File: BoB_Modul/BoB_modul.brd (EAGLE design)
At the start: 27.9 x 40.6 mm, 12 parts

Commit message: make metric and nice, not yet finnished, work in progress
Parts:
- moved C3 0.79 mm to (22.5, 17.5)
- moved X1 0.54 mm to (14.0, 40.1)
- moved R2 0.28 mm to (22.0, 10.0)
- moved C1 0.24 mm to (6.50, 4.00)
- moved R1 0.23 mm to (18.5, 5.50)
- moved C4 0.23 mm to (22.0, 7.00)
- moved LDO1 0.20 mm to (12.5, 7.00)
- moved SV2 0.16 mm to (25.5, 16.0)
- moved SV1 0.13 mm to (2.50, 16.0)
- moved LED1 0.09 mm to (18.5, 2.50)
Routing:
- net DBG_DATA_RX_LED: track 14.8 -> 0.00 mm, vias 1 -> 0
- net DBG_CLK_TX_LED: track 13.8 -> 0.00 mm, vias 1 -> 0
- net DBG_EN_NC: track 12.8 -> 0.00 mm, vias 1 -> 0
- net /RST: track 16.4 -> 15.3 mm
- net GND: track 45.9 -> 45.1 mm
- net GPIO2: track 8.24 -> 8.81 mm
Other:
- board size 27.9 x 40.6 mm -> 28 x 40 mm

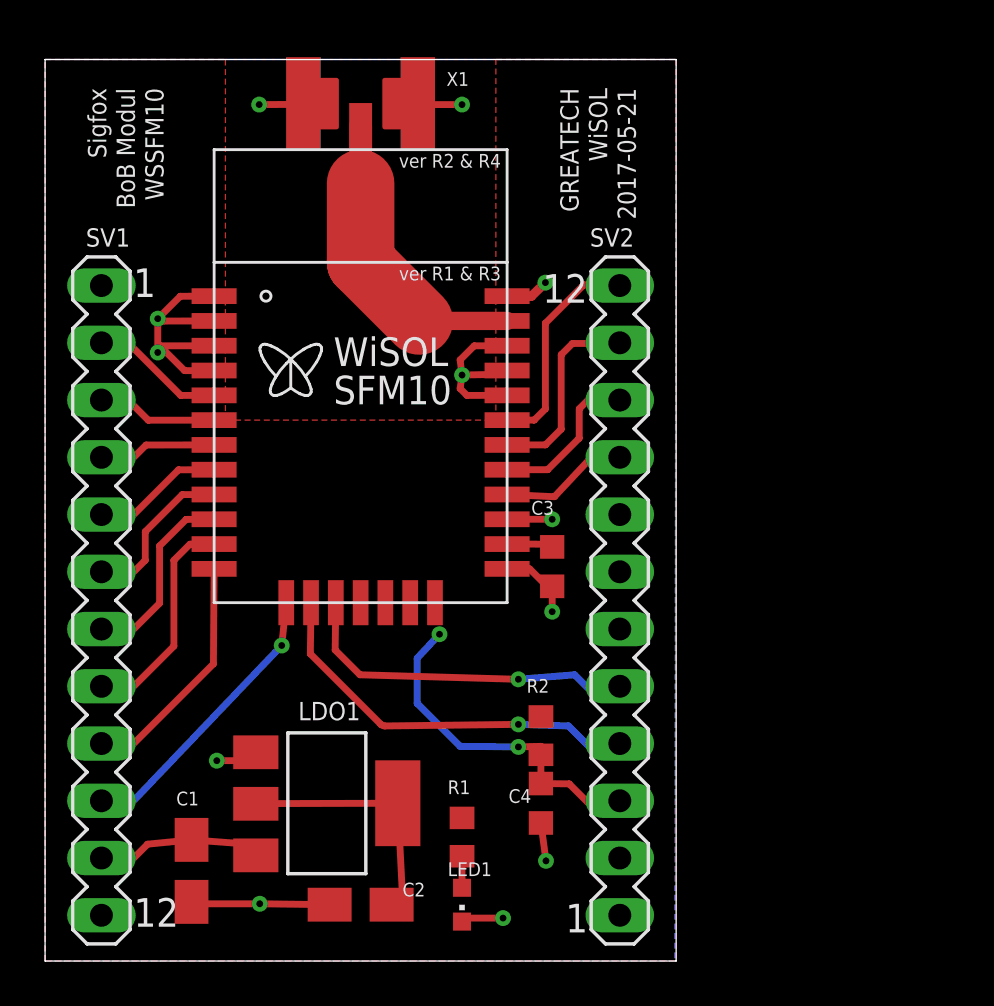
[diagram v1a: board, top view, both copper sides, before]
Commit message: make metric, moved vias out of WiSOL module, ready fro production
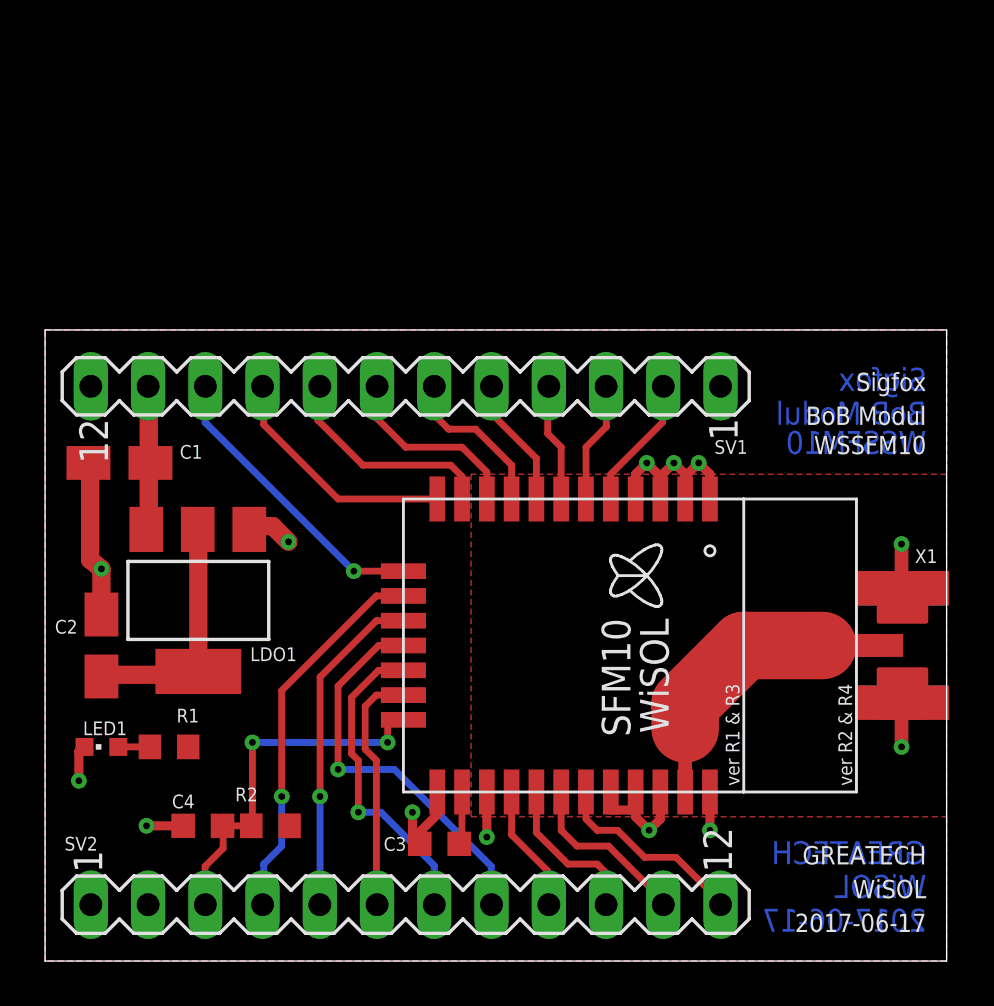
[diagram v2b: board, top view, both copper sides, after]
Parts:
- moved X1 36.9 mm to (40.1, 14.0), turned to 180 degrees
- moved C1 18.4 mm to (3.30, 22.1), turned to 0 degrees
- moved LED1 17.5 mm to (2.50, 9.50), turned to 90 degrees
- moved SV1 16.5 mm to (16.0, 25.5), turned to 180 degrees
- moved SV2 16.5 mm to (16.0, 2.50), turned to 0 degrees
- moved C2 16.3 mm to (2.50, 14.0), turned to 270 degrees
- moved C4 15.0 mm to (7.00, 6.00), turned to 180 degrees
- moved R1 13.6 mm to (5.50, 9.50), turned to 0 degrees
- moved WSSFM10 13.4 mm to (23.5, 14.0), turned to 270 degrees
- moved C3 13.3 mm to (17.5, 5.20), turned to 180 degrees
- moved R2 12.6 mm to (10.0, 6.00), turned to 0 degrees
- moved LDO1 10.7 mm to (6.80, 16.0), turned to 180 degrees
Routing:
- net DBG_DATA_RX_LED: track 0.00 -> 17.6 mm, vias 0 -> 1
- net DBG_CLK_TX_LED: track 0.00 -> 14.1 mm, vias 0 -> 1
- net DBG_EN_NC: track 0.00 -> 10.9 mm
- net GND: track 45.1 -> 41.2 mm, vias 12 -> 13
- net /RST: track 15.3 -> 16.4 mm
- net GPIO2: track 8.81 -> 7.70 mm
- net GPIO3: track 9.71 -> 8.80 mm
- net TX: track 17.7 -> 17.0 mm
- net 5V: track 7.45 -> 6.78 mm
- net RX: track 15.5 -> 14.8 mm
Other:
- board size 28 x 40 mm -> 40 x 28 mm
- board text added: "2017-06-17"
- board text removed: "2017-05-21"
